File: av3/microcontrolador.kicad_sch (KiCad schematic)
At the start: 36 parts, among them J1 DE9_Pins_MountingHoles, J16 Screw_Terminal_01x03, J9 Conn_02x05_Odd_Even, SW1 SW_MEC_5G, U1 ATmega2560-16A, U10 LCD-016N002L, U2 6N137, U7 6N137, U9 MAX232, Y1 16Mhz

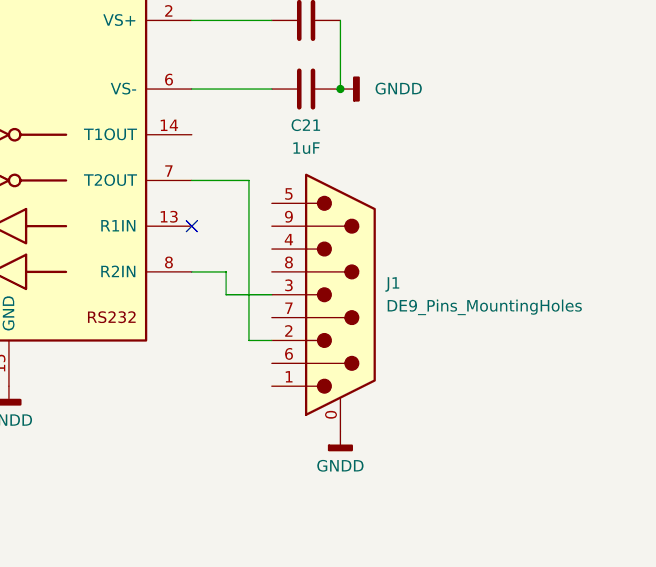
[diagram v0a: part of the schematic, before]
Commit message: FEAT: Adição das footprints dos capacitores (C) e screw_terminals (J)
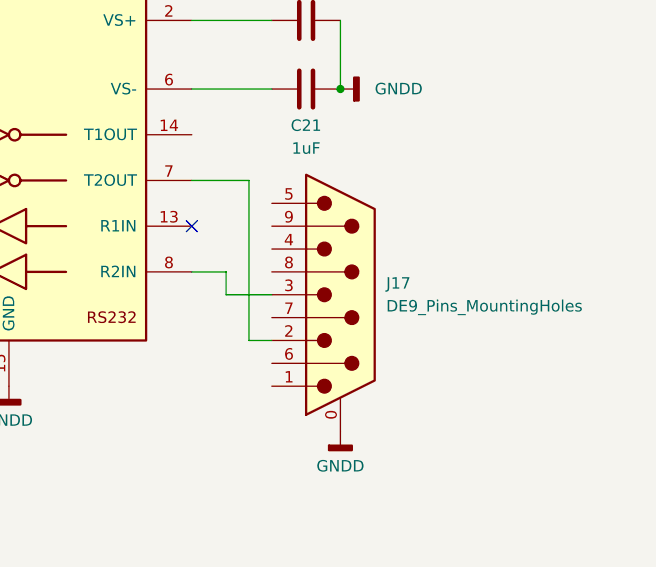
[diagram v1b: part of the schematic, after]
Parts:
- C1, C12, C13, C16, C17, C2, C22, C23, C24, C3, C4, C5: footprint (none) -> Capacitor_SMD:C_0805_2012Metric
- C14, C15: footprint (none) -> Capacitor_THT:CP_Radial_D5.0mm_P2.50mm
- C18, C19, C20, C21: footprint (none) -> Capacitor_THT:CP_Radial_D4.0mm_P2.00mm
- J16: footprint (none) -> TerminalBlock:TerminalBlock_MaiXu_MX126-5.0-03P_1x03_P5.00mm
- J9: footprint (none) -> Connector_PinHeader_2.54mm:PinHeader_2x05_P2.54mm_Vertical
- renumbered J1 to J17
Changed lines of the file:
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@@
 			)
 		)
-		(property "Footprint" ""
+		(property "Footprint" "Capacitor_SMD:C_0805_2012Metric"
 			(at 166.37 56.1848 0)
 			(effects
@@
 			)
 		)
-		(property "Footprint" ""
+		(property "Footprint" "Capacitor_SMD:C_0805_2012Metric"
 			(at 36.83 46.0248 0)
 			(effects
@@
 			)
 		)
-		(property "Footprint" ""
+		(property "Footprint" "Capacitor_THT:CP_Radial_D4.0mm_P2.00mm"
 			(at 252.4252 109.22 0)
 			(effects
@@
 			)
 		)
-		(property "Footprint" ""
+		(property "Footprint" "Capacitor_SMD:C_0805_2012Metric"
 			(at 44.45 46.0248 0)
 			(effects
@@
 			)
 		)
-		(property "Footprint" ""
+		(property "Footprint" "Capacitor_SMD:C_0805_2012Metric"
 			(at 279.4 89.2048 0)
 			(effects
@@
 			)
 		)
-		(property "Footprint" ""
+		(property "Footprint" "Capacitor_SMD:C_0805_2012Metric"
 			(at 130.5052 60.96 0)
 			(effects
@@
 			)
 		)
-		(property "Footprint" ""
+		(property "Footprint" "Capacitor_THT:CP_Radial_D4.0mm_P2.00mm"
 			(at 308.61 120.9548 0)
 			(effects
@@
 			)
 		)
-		(property "Footprint" ""
+		(property "Footprint" "Capacitor_THT:CP_Radial_D4.0mm_P2.00mm"
 			(at 293.0652 109.22 0)
 			(effects
@@
 			)
 		)
-		(property "Footprint" ""
+		(property "Footprint" "Capacitor_SMD:C_0805_2012Metric"
 			(at 139.7 81.5848 0)
 			(effects
@@
 			)
 		)
-		(property "Footprint" ""
+		(property "Footprint" "TerminalBlock:TerminalBlock_MaiXu_MX126-5.0-03P_1x03_P5.00mm"
 			(at 36.83 21.59 0)
 			(effects
@@
 			)
 		)
-		(property "Footprint" ""
+		(property "Footprint" "Capacitor_THT:CP_Radial_D4.0mm_P2.00mm"
 			(at 308.61 113.3348 0)
 			(effects
@@
 			)
 		)
-		(property "Footprint" ""
+		(property "Footprint" "Capacitor_THT:CP_Radial_D5.0mm_P2.50mm"
 			(at 44.45 37.1348 0)
 			(effects
@@
 			)
 		)
-		(property "Footprint" ""
+		(property "Footprint" "Capacitor_SMD:C_0805_2012Metric"
 			(at 231.14 95.5548 0)
 			(effects
@@
 			)
 		)
-		(property "Footprint" ""
+		(property "Footprint" "Capacitor_SMD:C_0805_2012Metric"
 			(at 254.9652 74.93 0)
 			(effects
@@
 		(dnp no)
 		(fields_autoplaced yes)
-		(property "Reference" "J1"
+		(property "Reference" "J17"
 			(at 313.69 143.5099 0)
 			(effects
@@
 			(project ""
 				(path "/a93ad2d2-2340-43ed-bd19-332540d0678c/ed344d39-63c7-463e-a8dd-63e00df6567a"
-					(reference "J1")
+					(reference "J17")
 					(unit 1)
 				)
@@
 			)
 		)
-		(property "Footprint" ""
+		(property "Footprint" "Capacitor_SMD:C_0805_2012Metric"
 			(at 173.99 56.1848 0)
 			(effects
@@
 			)
 		)
-		(property "Footprint" ""
+		(property "Footprint" "Capacitor_SMD:C_0805_2012Metric"
 			(at 296.8752 74.93 0)
 			(effects
@@
 			)
 		)
-		(property "Footprint" ""
+		(property "Footprint" "Connector_PinHeader_2.54mm:PinHeader_2x05_P2.54mm_Vertical"
 			(at 109.22 91.44 0)
 			(effects
@@
 			)
 		)
-		(property "Footprint" ""
+		(property "Footprint" "Capacitor_SMD:C_0805_2012Metric"
 			(at 139.7 73.9648 0)
 			(effects
@@
 			)
 		)
-		(property "Footprint" ""
+		(property "Footprint" "Capacitor_THT:CP_Radial_D5.0mm_P2.50mm"
 			(at 36.83 37.1348 0)
 			(effects
@@
 			)
 		)
-		(property "Footprint" ""
+		(property "Footprint" "Capacitor_SMD:C_0805_2012Metric"
 			(at 223.52 133.6548 0)
 			(effects

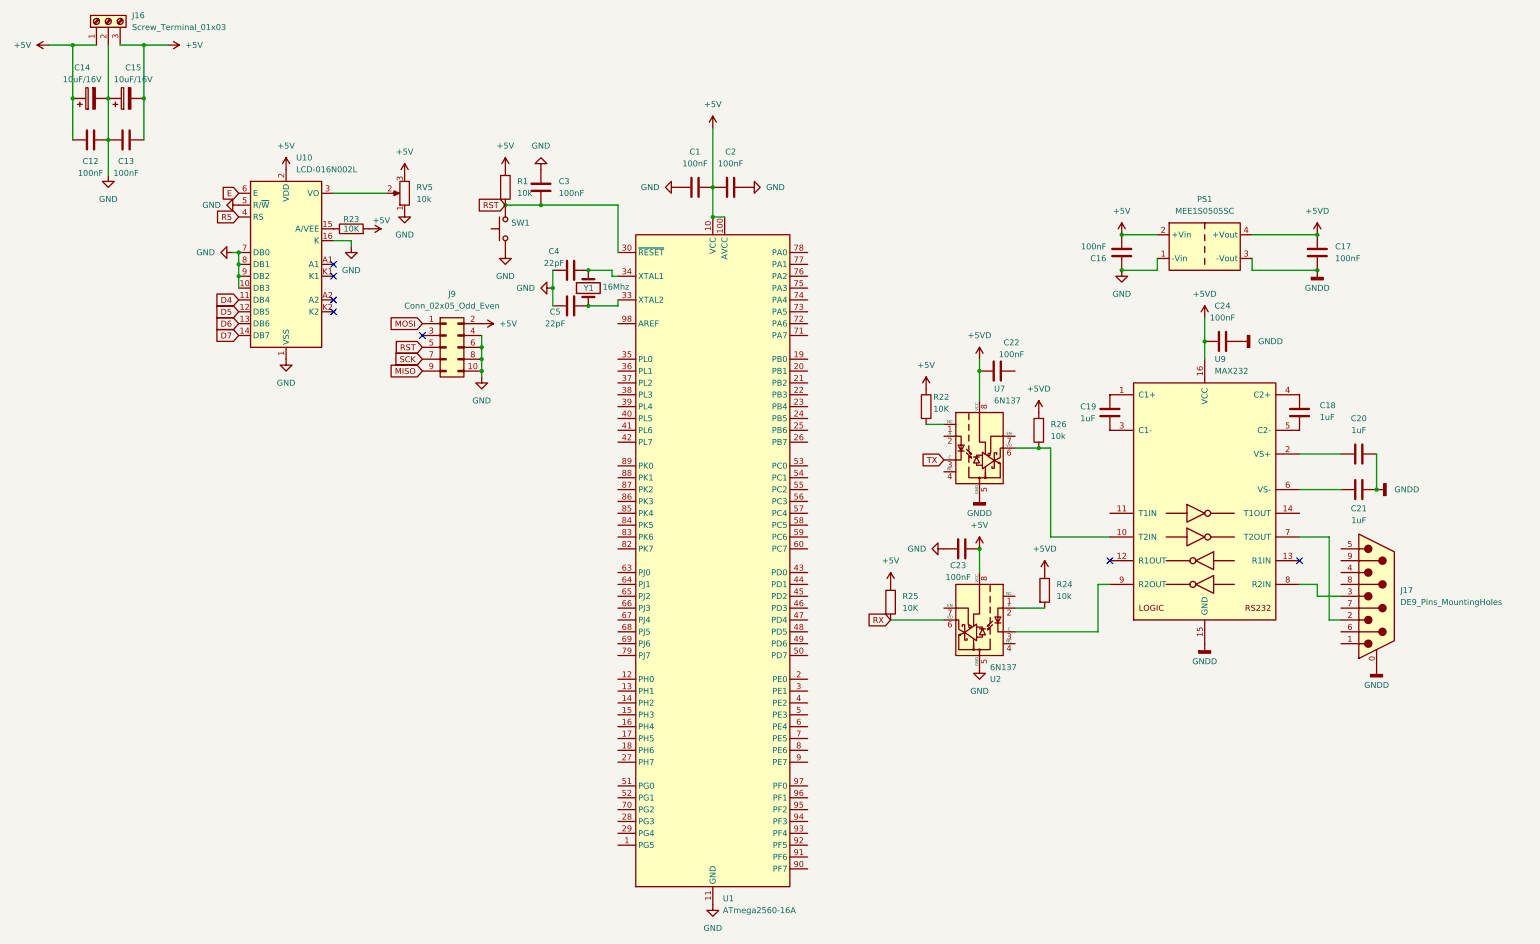
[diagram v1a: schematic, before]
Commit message: Alteração do footprint do PS1 e inicio da PCB
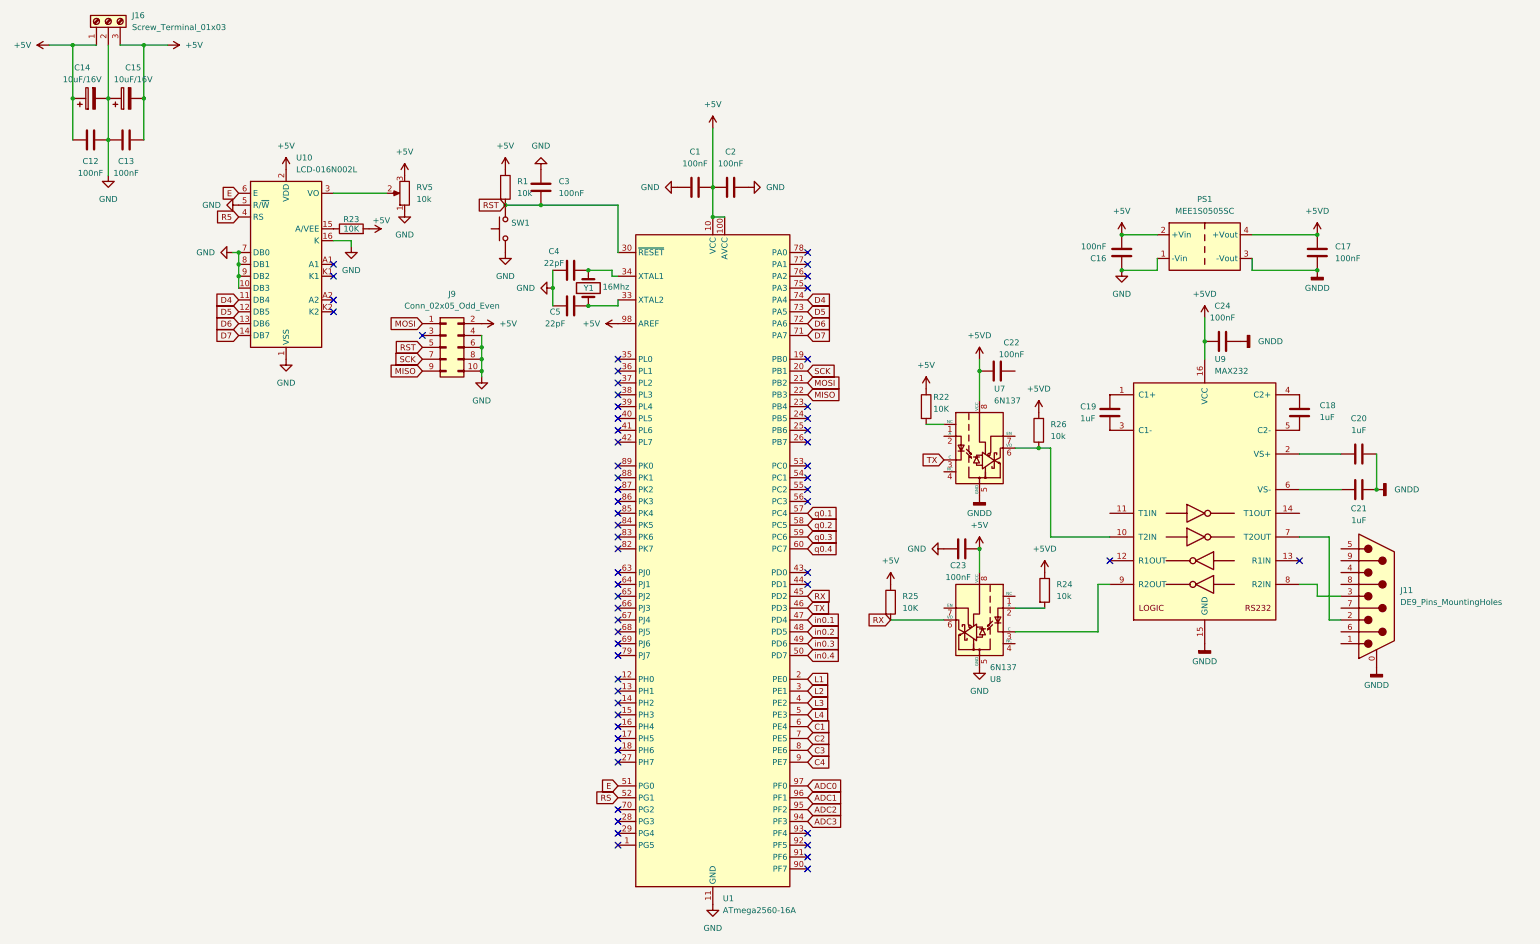
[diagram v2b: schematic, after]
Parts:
- J11: renamed from J17; footprint (none) -> Connector_Dsub:DSUB-9_Pins_Vertical_P2.77x2.84mm_MountingHoles
- J16: footprint TerminalBlock:TerminalBlock_MaiXu_MX126-5.0-03P_1x03_P5.00mm -> TerminalBlock_Phoenix:TerminalBlock_Phoenix_MKDS-1,5-3-5.08_1x03_P5.08mm_Horizontal
- PS1: footprint Converter_DCDC:Converter_DCDC_Murata_MEE1SxxxxSC_THT -> Converter_DCDC:Converter_DCDC_Murata_CRE1xxxxxxSC_THT
- R1, R22, R23, R24, R25, R26, RV5: footprint (none) -> Resistor_THT:R_Axial_DIN0207_L6.3mm_D2.5mm_P7.62mm_Horizontal
- SW1: footprint (none) -> Button_Switch_SMD:SW_Push_1P1T_NO_CK_KSC7xxJ
- U9: footprint (none) -> Package_DIP:DIP-16_W7.62mm
- Y1: footprint (none) -> Crystal:Resonator-2Pin_W10.0mm_H5.0mm
- renumbered U2 to U8
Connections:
- net +5V: now also U1.98 (AREF)
- net D4: now also U1.74 (PA4)
- net D5: now also U1.73 (PA5)
- net D6: now also U1.72 (PA6)
- net D7: now also U1.71 (PA7)
- net E: now also U1.51 (PG0)
- net MISO: now also U1.22 (PB3)
- net MOSI: now also U1.21 (PB2)
- net RX: now also U1.45 (PD2)
- net SCK: now also U1.20 (PB1)
- net TX: now also U1.46 (PD3)
- net L1: now reaches U1.2 (PE0)
- net L2: now reaches U1.3 (PE1)
- net L3: now reaches U1.4 (PE2)
- net in0.1: now reaches U1.47 (PD4)
- net in0.2: now reaches U1.48 (PD5)
- net in0.3: now reaches U1.49 (PD6)
- net L4: now reaches U1.5 (PE3)
- net in0.4: now reaches U1.50 (PD7)
- net RS: now reaches U1.52 (PG1)
- net q0.1: now reaches U1.57 (PC4)
- net q0.2: now reaches U1.58 (PC5)
- net q0.3: now reaches U1.59 (PC6)
- net C1: now reaches U1.6 (PE4)
- net q0.4: now reaches U1.60 (PC7)
- net C2: now reaches U1.7 (PE5)
- net C3: now reaches U1.8 (PE6)
- net C4: now reaches U1.9 (PE7)
- net ADC3: now reaches U1.94 (PF3)
- net ADC2: now reaches U1.95 (PF2)
- net ADC1: now reaches U1.96 (PF1)
- net ADC0: now reaches U1.97 (PF0)
- no-connect marks 7 -> 62

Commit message: Mudança de footprints e mudança na PCB
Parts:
- RV5: footprint Resistor_THT:R_Axial_DIN0207_L6.3mm_D2.5mm_P7.62mm_Horizontal -> Potentiometer_THT:Potentiometer_Bourns_3296W_Vertical
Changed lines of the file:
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@@
 			)
 		)
-		(property "Footprint" "Resistor_THT:R_Axial_DIN0207_L6.3mm_D2.5mm_P7.62mm_Horizontal"
+		(property "Footprint" "Potentiometer_THT:Potentiometer_Bourns_3296W_Vertical"
 			(at 100.33 58.42 0)
 			(effects

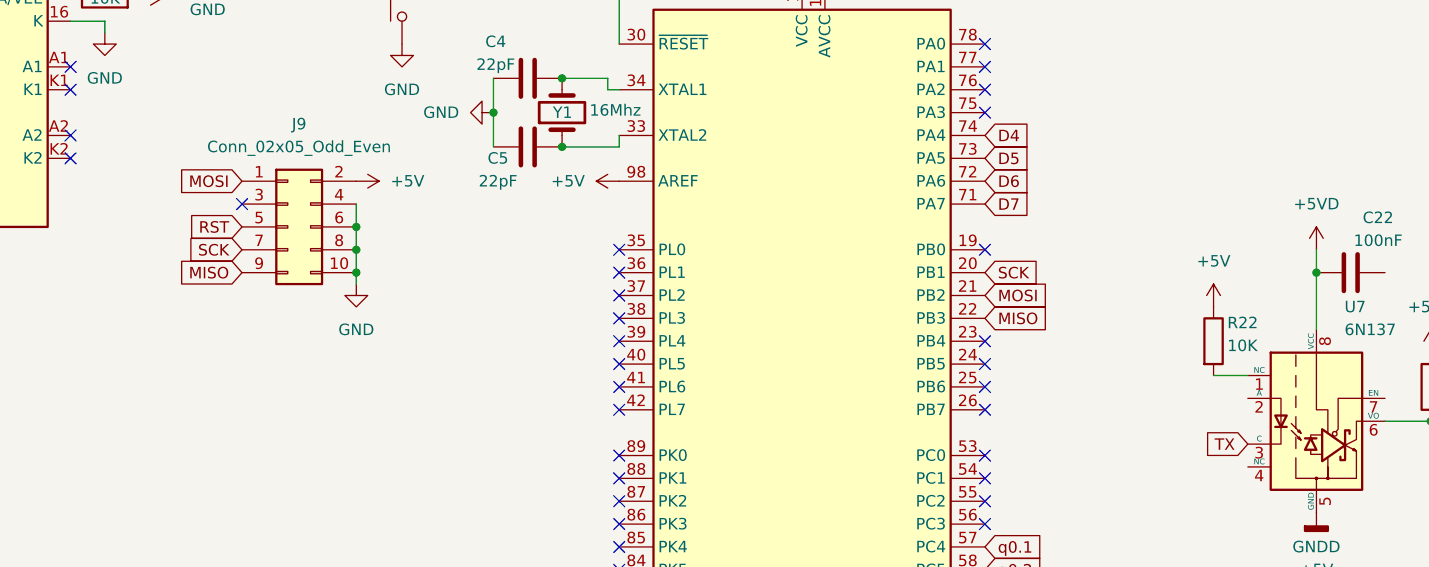
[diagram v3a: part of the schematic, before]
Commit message: Finaliza a organização dos componentes na PCB, ajusta footprints
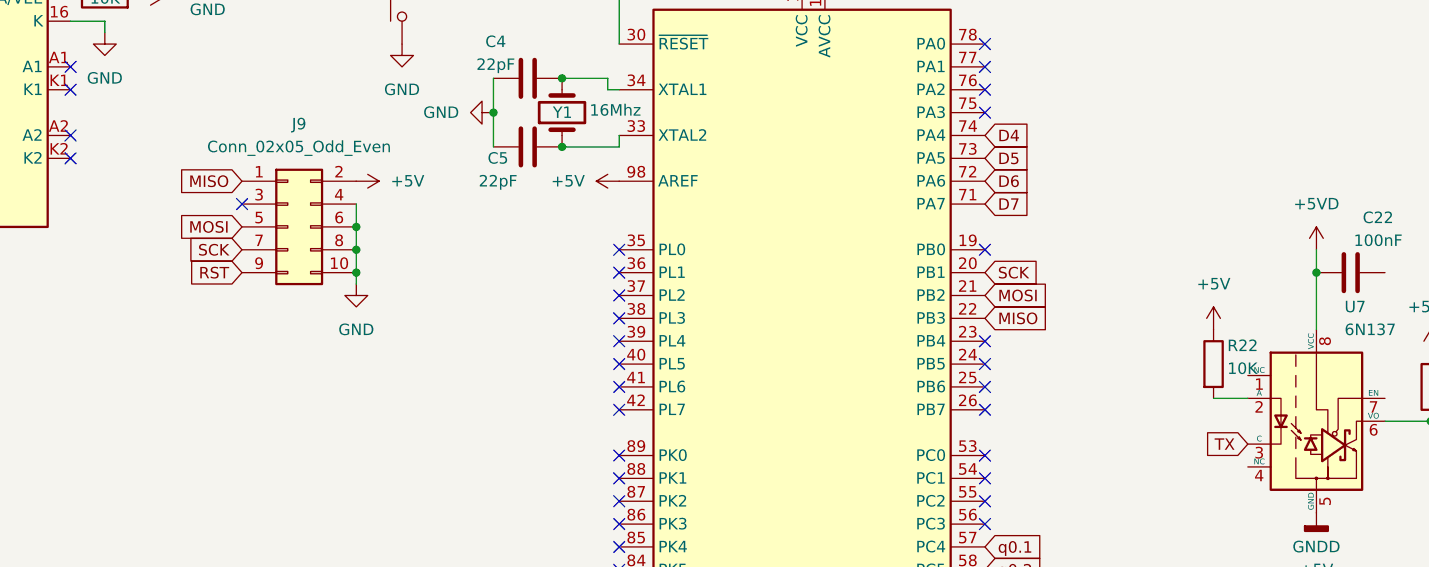
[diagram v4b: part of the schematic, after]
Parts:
- removed SW1: SW_MEC_5G, Button_Switch_SMD:SW_Push_1P1T_NO_CK_KSC7xxJ, symbol Switch:SW_MEC_5G
- added SW1: SW_Omron_B3FS, Button_Switch_SMD:SW_Push_1P1T_NO_CK_KSC7xxJ, symbol Switch:SW_Omron_B3FS
- C18, C19, C20, C21: footprint Capacitor_THT:CP_Radial_D4.0mm_P2.00mm -> Capacitor_SMD:C_0805_2012Metric
- J9: footprint Connector_PinHeader_2.54mm:PinHeader_2x05_P2.54mm_Vertical -> Connector_IDC:IDC-Header_2x05_P2.54mm_Vertical
- R1, R22, R23, R24, R25, R26: footprint Resistor_THT:R_Axial_DIN0207_L6.3mm_D2.5mm_P7.62mm_Horizontal -> Resistor_SMD:R_0805_2012Metric
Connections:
- net GND: now also SW1.1
- net MISO: now also J9.1 (Pin_1); no longer J9.9 (Pin_9)
- net MOSI: now also J9.5 (Pin_5); no longer J9.1 (Pin_1)
- net RST: now also J9.9 (Pin_9), SW1.2; no longer J9.5 (Pin_5)
- net at U7.1 (NC): no longer R22.2
- net at U7.2 (A): now also R22.2
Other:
- moved on the sheet: R22
